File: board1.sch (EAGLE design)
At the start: 7 parts

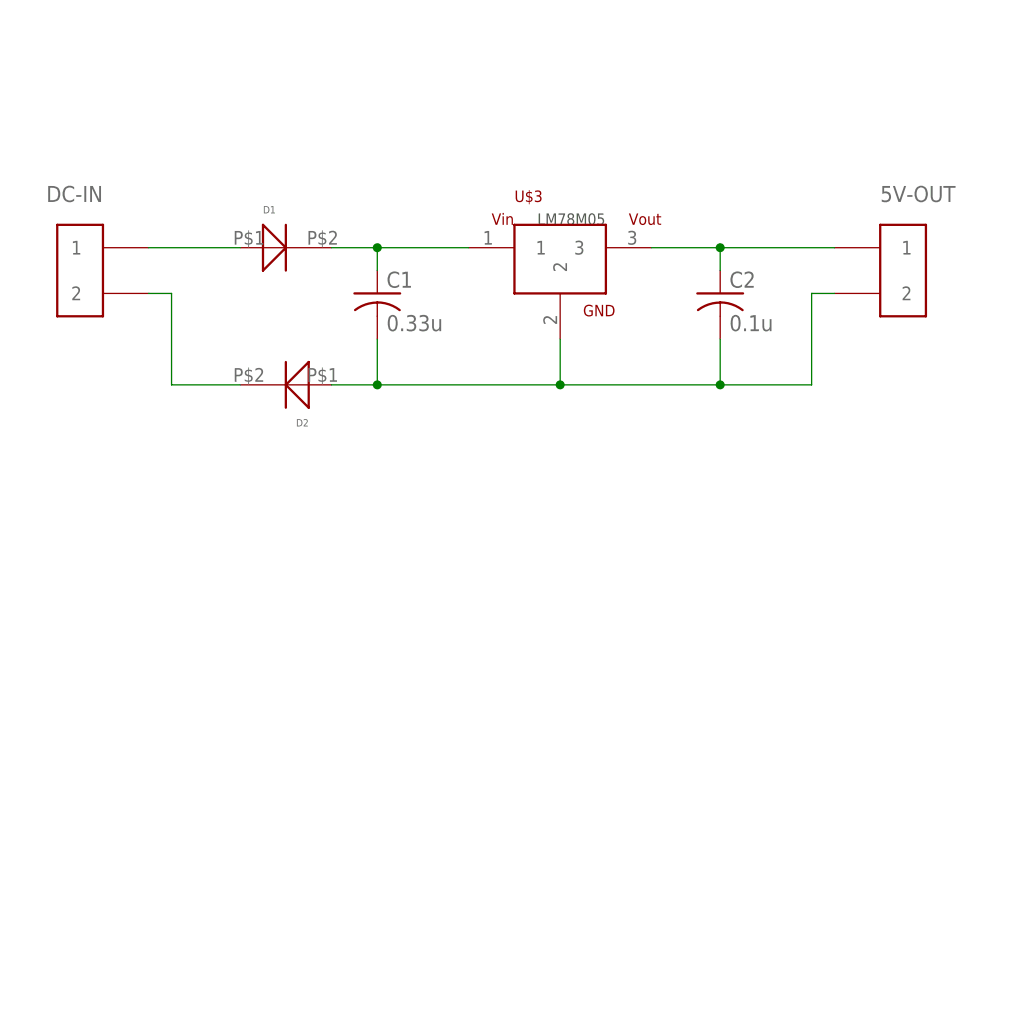
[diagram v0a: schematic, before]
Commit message: Final version. Added also vias for soldering external the sensor (maybe we will remove them)
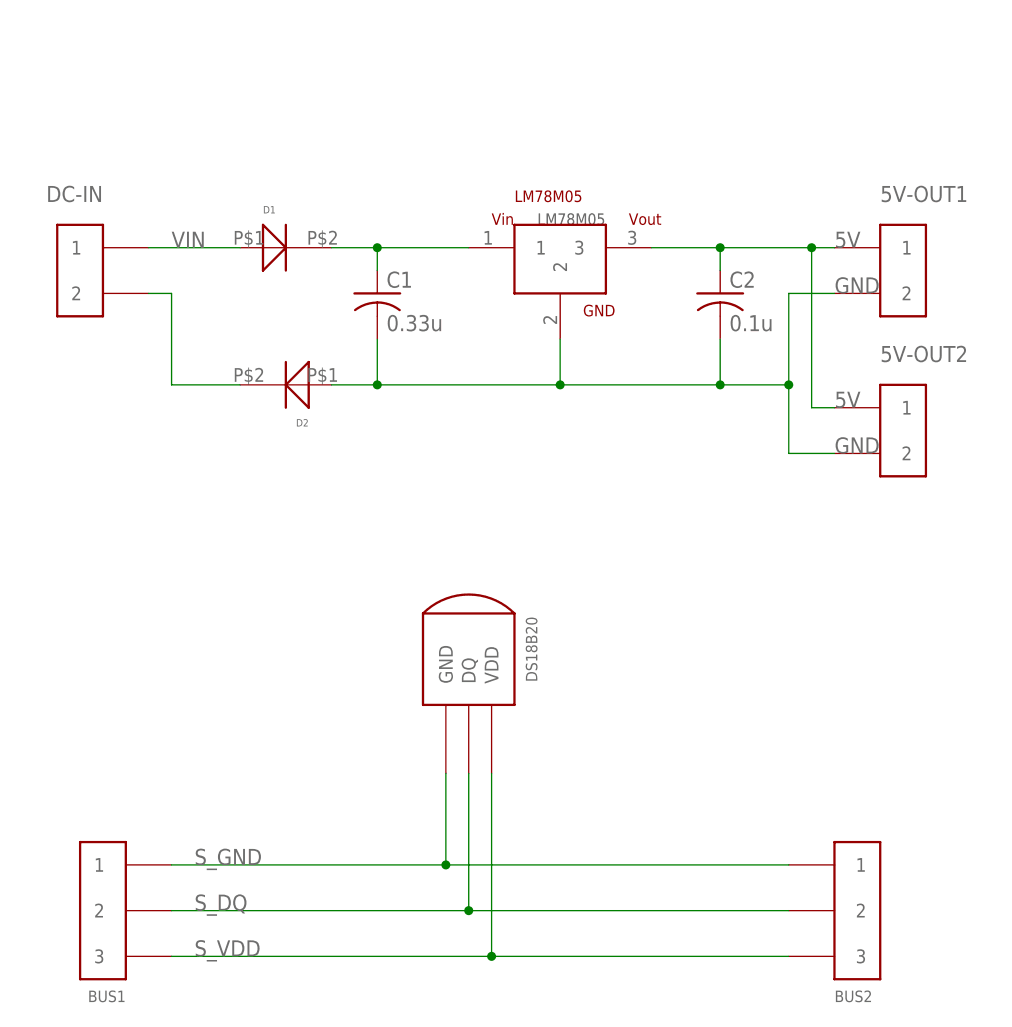
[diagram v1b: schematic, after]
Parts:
- added 5V-OUT2: 2PIN-TERMINAL-5MMPITCH, Paschalis_connectors:2PIN-TERMINAL-5MMPITCH
- added BUS1, BUS2: AVX-3PIN-SMD-CON, Paschalis_connectors:AVX-3PIN-SMD-CON
- added DS18B20: SMD-3PAD-DS18B20, Paschalis_connectors:SMD-3PAD-DS18B20
- renumbered 5V-OUT to 5V-OUT1, U$3 to LM78M05
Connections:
- net N$1 renamed VIN
- removed net N$3: 5V-OUT1.2, C1.2, C2.2, D2.1, LM78M05.2
- removed net N$5: 5V-OUT1.1, C2.1, LM78M05.3
- new net 5V: 5V-OUT1.1, 5V-OUT2.1, C2.1, LM78M05.3
- new net GND: 5V-OUT1.2, 5V-OUT2.2, C1.2, C2.2, D2.1, LM78M05.2
- new net S_DQ: BUS1.2, BUS2.2, DS18B20.DQ
- new net S_GND: BUS1.1, BUS2.1, DS18B20.GND
- new net S_VDD: BUS1.3, BUS2.3, DS18B20.VDD
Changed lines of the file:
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@@
 <parts>
 <part name="DC-IN" library="Paschalis_connectors" deviceset="2PIN-TERMINAL-5MMPITCH" device=""/>
-<part name="5V-OUT" library="Paschalis_connectors" deviceset="2PIN-TERMINAL-5MMPITCH" device=""/>
+<part name="5V-OUT1" library="Paschalis_connectors" deviceset="2PIN-TERMINAL-5MMPITCH" device=""/>
 <part name="C1" library="adafruit" deviceset="C-US" device="C3216" value="0.33u"/>
 <part name="C2" library="adafruit" deviceset="C-US" device="C3216" value="0.1u"/>
 <part name="D1" library="Bart_educatief_aanbod" deviceset="DIODE" device=""/>
 <part name="D2" library="Bart_educatief_aanbod" deviceset="DIODE" device=""/>
-<part name="U$3" library="Bart_educatief_aanbod" deviceset="LM78M05" device=""/>
+<part name="LM78M05" library="Bart_educatief_aanbod" deviceset="LM78M05" device=""/>
+<part name="BUS1" library="Paschalis_connectors" deviceset="AVX-3PIN-SMD-CON" device=""/>
+<part name="BUS2" library="Paschalis_connectors" deviceset="AVX-3PIN-SMD-CON" device=""/>
+<part name="DS18B20" library="Paschalis_connectors" deviceset="SMD-3PAD-DS18B20" device=""/>
+<part name="5V-OUT2" library="Paschalis_connectors" deviceset="2PIN-TERMINAL-5MMPITCH" device=""/>
 </parts>
 <sheets>
@@
 <instances>
 <instance part="DC-IN" gate="G$1" x="15.24" y="101.6" rot="MR0"/>
-<instance part="5V-OUT" gate="G$1" x="106.68" y="101.6"/>
+<instance part="5V-OUT1" gate="G$1" x="106.68" y="101.6"/>
 <instance part="C1" gate="G$1" x="48.26" y="99.06"/>
 <instance part="C2" gate="G$1" x="86.36" y="99.06"/>
 <instance part="D1" gate="G$1" x="38.1" y="104.14"/>
 <instance part="D2" gate="G$1" x="38.1" y="88.9" rot="R180"/>
-<instance part="U$3" gate="G$1" x="68.58" y="101.6"/>
+<instance part="LM78M05" gate="G$1" x="68.58" y="101.6"/>
+<instance part="BUS1" gate="G$1" x="17.78" y="30.48" rot="MR0"/>
+<instance part="BUS2" gate="G$1" x="101.6" y="30.48"/>
+<instance part="DS18B20" gate="G$1" x="58.42" y="58.42"/>
+<instance part="5V-OUT2" gate="G$1" x="106.68" y="83.82"/>
 </instances>
 <busses>
 </busses>
 <nets>
-<net name="N$1" class="0">
+<net name="VIN" class="0">
 <segment>
 <pinref part="DC-IN" gate="G$1" pin="1"/>
 <pinref part="D1" gate="G$1" pin="1"/>
 <wire x1="22.86" y1="104.14" x2="33.02" y2="104.14" width="0.1524" layer="91"/>
+<label x="25.4" y="104.14" size="1.778" layer="95"/>
 </segment>
 </net>
@@
 <segment>
 <pinref part="D1" gate="G$1" pin="2"/>
-<pinref part="U$3" gate="G$1" pin="1"/>
+<pinref part="LM78M05" gate="G$1" pin="1"/>
 <wire x1="43.18" y1="104.14" x2="48.26" y2="104.14" width="0.1524" layer="91"/>
 <pinref part="C1" gate="G$1" pin="1"/>
@@
 </segment>
 </net>
-<net name="N$3" class="0">
+<net name="GND" class="0">
 <segment>
-<pinref part="U$3" gate="G$1" pin="2"/>
+<pinref part="LM78M05" gate="G$1" pin="2"/>
 <wire x1="68.58" y1="93.98" x2="68.58" y2="88.9" width="0.1524" layer="91"/>
 <pinref part="D2" gate="G$1" pin="1"/>
@@
 <junction x="48.26" y="88.9"/>
 <wire x1="68.58" y1="88.9" x2="86.36" y2="88.9" width="0.1524" layer="91"/>
-<wire x1="86.36" y1="88.9" x2="96.52" y2="88.9" width="0.1524" layer="91"/>
-<wire x1="96.52" y1="88.9" x2="96.52" y2="99.06" width="0.1524" layer="91"/>
+<wire x1="86.36" y1="88.9" x2="93.98" y2="88.9" width="0.1524" layer="91"/>
+<wire x1="93.98" y1="88.9" x2="93.98" y2="99.06" width="0.1524" layer="91"/>
 <junction x="68.58" y="88.9"/>
-<pinref part="5V-OUT" gate="G$1" pin="2"/>
-<wire x1="96.52" y1="99.06" x2="99.06" y2="99.06" width="0.1524" layer="91"/>
+<pinref part="5V-OUT1" gate="G$1" pin="2"/>
+<wire x1="93.98" y1="99.06" x2="99.06" y2="99.06" width="0.1524" layer="91"/>
 <pinref part="C2" gate="G$1" pin="2"/>
 <wire x1="86.36" y1="93.98" x2="86.36" y2="88.9" width="0.1524" layer="91"/>
 <junction x="86.36" y="88.9"/>
+<wire x1="93.98" y1="88.9" x2="93.98" y2="81.28" width="0.1524" layer="91"/>
+<junction x="93.98" y="88.9"/>
+<pinref part="5V-OUT2" gate="G$1" pin="2"/>
+<wire x1="93.98" y1="81.28" x2="99.06" y2="81.28" width="0.1524" layer="91"/>
+<label x="99.06" y="99.06" size="1.778" layer="95"/>
+<label x="99.06" y="81.28" size="1.778" layer="95"/>
 </segment>
 </net>
@@
 </segment>
 </net>
-<net name="N$5" class="0">
+<net name="5V" class="0">
 <segment>
-<pinref part="U$3" gate="G$1" pin="3"/>
-<pinref part="5V-OUT" gate="G$1" pin="1"/>
+<pinref part="LM78M05" gate="G$1" pin="3"/>
+<pinref part="5V-OUT1" gate="G$1" pin="1"/>
 <wire x1="78.74" y1="104.14" x2="86.36" y2="104.14" width="0.1524" layer="91"/>
 <pinref part="C2" gate="G$1" pin="1"/>
-<wire x1="86.36" y1="104.14" x2="99.06" y2="104.14" width="0.1524" layer="91"/>
+<wire x1="86.36" y1="104.14" x2="96.52" y2="104.14" width="0.1524" layer="91"/>
+<wire x1="96.52" y1="104.14" x2="99.06" y2="104.14" width="0.1524" layer="91"/>
 <wire x1="86.36" y1="101.6" x2="86.36" y2="104.14" width="0.1524" layer="91"/>
 <junction x="86.36" y="104.14"/>
+<wire x1="96.52" y1="104.14" x2="96.52" y2="86.36" width="0.1524" layer="91"/>
+<junction x="96.52" y="104.14"/>
+<pinref part="5V-OUT2" gate="G$1" pin="1"/>
+<wire x1="96.52" y1="86.36" x2="99.06" y2="86.36" width="0.1524" layer="91"/>
+<label x="99.06" y="104.14" size="1.778" layer="95"/>
+<label x="99.06" y="86.36" size="1.778" layer="95"/>
 </segment>
 </net>
+<net name="S_GND" class="0">
+<segment>
+<pinref part="BUS1" gate="G$1" pin="1"/>
+<wire x1="25.4" y1="35.56" x2="55.88" y2="35.56" width="0.1524" layer="91"/>
+<pinref part="BUS2" gate="G$1" pin="1"/>
+<pinref part="DS18B20" gate="G$1" pin="GND"/>
+<wire x1="55.88" y1="35.56" x2="93.98" y2="35.56" width="0.1524" layer="91"/>
+<wire x1="55.88" y1="45.72" x2="55.88" y2="35.56" width="0.1524" layer="91"/>
+<junction x="55.88" y="35.56"/>
+<label x="27.94" y="35.56" size="1.778" layer="95"/>
+</segment>
+</net>
+<net name="S_DQ" class="0">
+<segment>
+<pinref part="BUS2" gate="G$1" pin="2"/>
+<pinref part="BUS1" gate="G$1" pin="2"/>
+<wire x1="93.98" y1="30.48" x2="58.42" y2="30.48" width="0.1524" layer="91"/>
+<pinref part="DS18B20" gate="G$1" pin="DQ"/>
+<wire x1="58.42" y1="30.48" x2="25.4" y2="30.48" width="0.1524" layer="91"/>
+<wire x1="58.42" y1="45.72" x2="58.42" y2="30.48" width="0.1524" layer="91"/>
+<junction x="58.42" y="30.48"/>
+<label x="27.94" y="30.48" size="1.778" layer="95"/>
+</segment>
+</net>
+<net name="S_VDD" class="0">
+<segment>
+<pinref part="BUS2" gate="G$1" pin="3"/>
+<pinref part="BUS1" gate="G$1" pin="3"/>
+<wire x1="93.98" y1="25.4" x2="60.96" y2="25.4" width="0.1524" layer="91"/>
+<pinref part="DS18B20" gate="G$1" pin="VDD"/>
+<wire x1="60.96" y1="25.4" x2="25.4" y2="25.4" width="0.1524" layer="91"/>
+<wire x1="60.96" y1="45.72" x2="60.96" y2="25.4" width="0.1524" layer="91"/>
+<junction x="60.96" y="25.4"/>
+<label x="27.94" y="25.4" size="1.778" layer="95"/>
+</segment>
+</net>

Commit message: Fixed the wrong path for bypass caps. Version v1.1
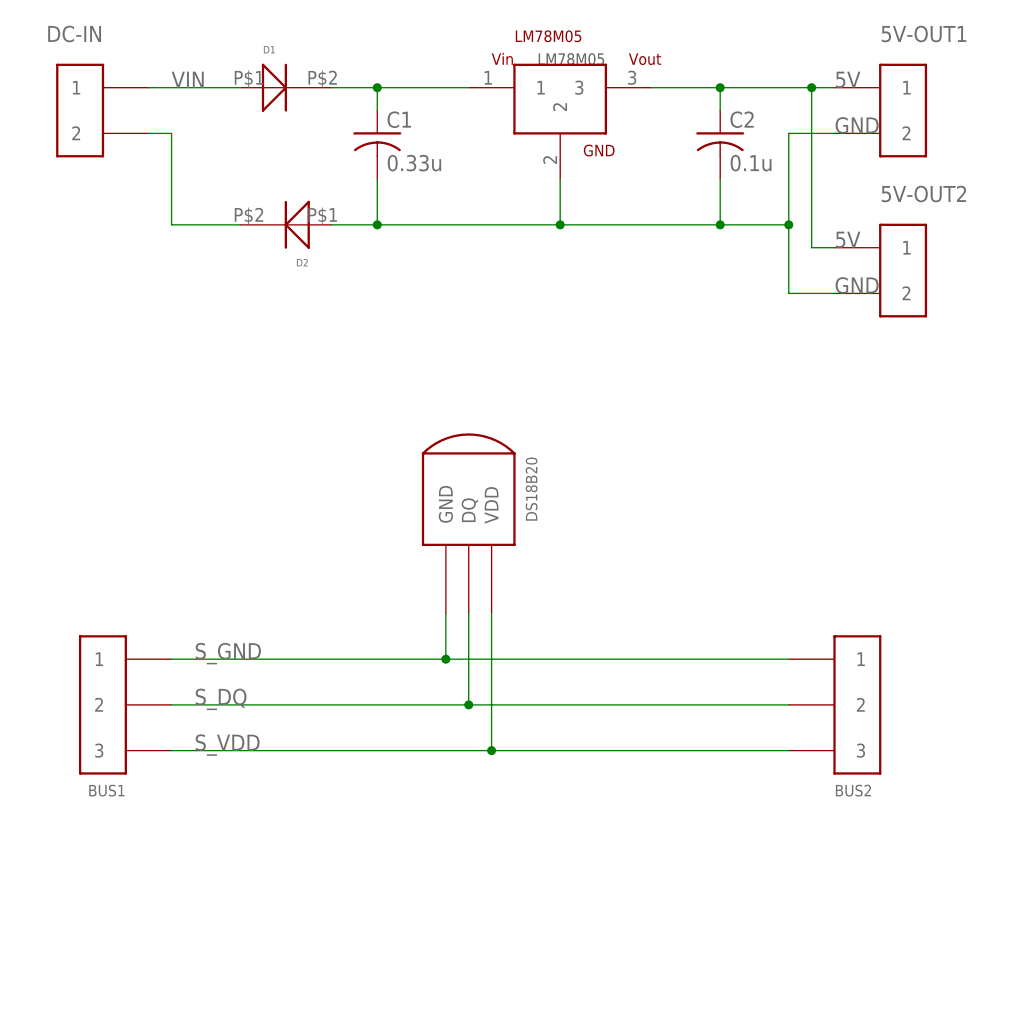
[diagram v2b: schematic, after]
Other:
- note added: "April 2016"
- note added: "IMEC KU Leuven"
- note added: "PowerTemp PCB"
- note added: "SIDE A: Voltage Regulation (7-30V to 5V) SIDE B: Temperature Sensor DS18B20 1Wire Bus"
- note added: "Sideridis Paschalis"
- note added: "date"
- note added: "description"
- note added: "designer"
- note added: "title"
- moved on the sheet: 5V-OUT1, 5V-OUT2, BUS1, BUS2, C1, C2, D1, D2, DC-IN, DS18B20, LM78M05
